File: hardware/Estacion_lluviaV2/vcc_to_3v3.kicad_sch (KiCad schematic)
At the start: 6 parts, among them U3 AMS1117-3.3

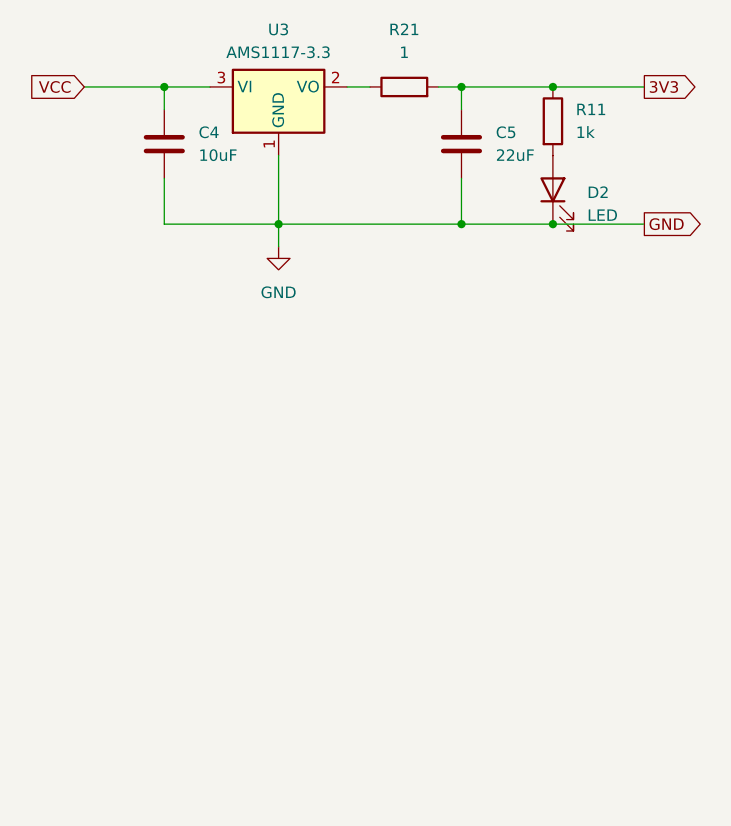
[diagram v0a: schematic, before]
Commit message: Se agregaron nuevos archivos
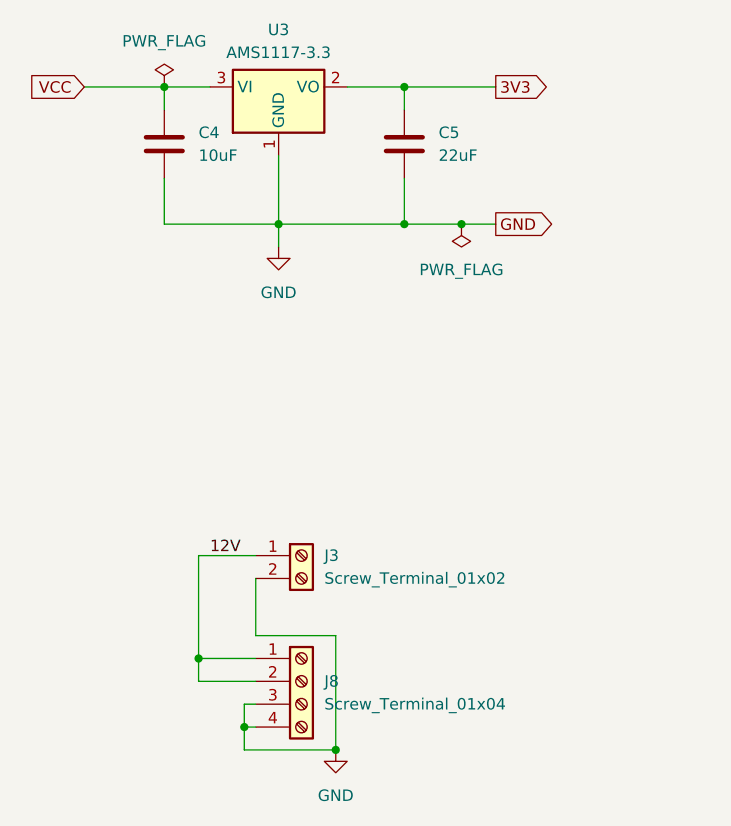
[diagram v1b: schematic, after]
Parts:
- removed D2: LED, LED_SMD:LED_0603_1608Metric, symbol Device:LED
- removed R11: 1k, Resistor_SMD:R_0603_1608Metric, symbol Device:R
- removed R21: 1, Resistor_SMD:R_0603_1608Metric, symbol Device:R
- added J3: Screw_Terminal_01x02, TerminalBlock:TerminalBlock_MaiXu_MX126-5.0-02P_1x02_P5.00mm, symbol Connector:Screw_Terminal_01x02
- added J8: Screw_Terminal_01x04, TerminalBlock:TerminalBlock_MaiXu_MX126-5.0-04P_1x04_P5.00mm, symbol Connector:Screw_Terminal_01x04
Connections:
- net 3V3: now also U3.2 (VO)
- net GND: now also J3.2 (Pin_2), J8.3 (Pin_3), J8.4 (Pin_4)
- new net 12V: J3.1 (Pin_1), J8.1 (Pin_1), J8.2 (Pin_2)
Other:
- moved on the sheet: C5
